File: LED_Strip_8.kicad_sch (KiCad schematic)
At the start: 8 parts

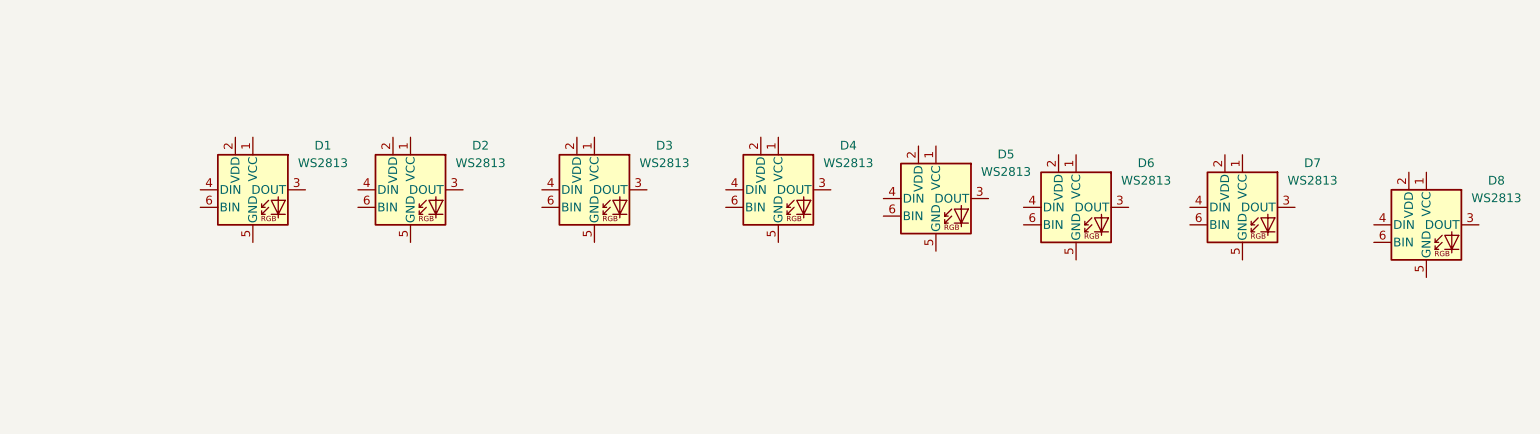
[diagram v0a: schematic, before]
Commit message: Wired LED strip
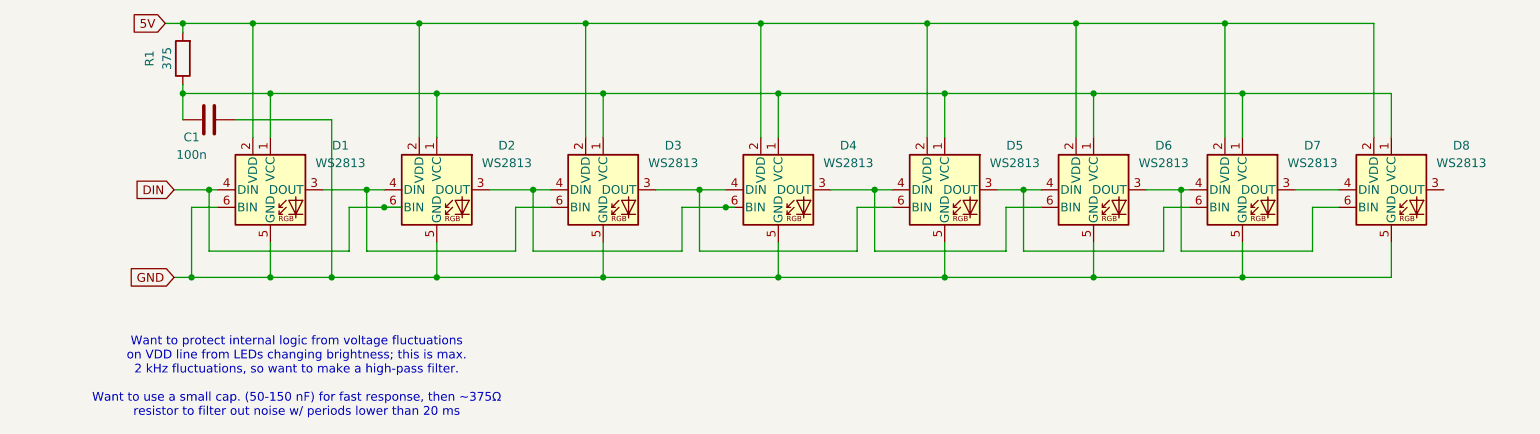
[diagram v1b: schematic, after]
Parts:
- added C1: 100n, symbol Device:C
- added R1: 375, symbol Device:R
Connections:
- net at D5.1 (VCC): now also D1.1 (VCC), D2.1 (VCC), D3.1 (VCC), D4.1 (VCC), D6.1 (VCC), D7.1 (VCC), D8.1 (VCC), C1.1, R1.1
- net 5V: now reaches D5.2 (VDD)
- net 5V: now also D1.2 (VDD), D2.2 (VDD), D3.2 (VDD), D4.2 (VDD), D6.2 (VDD), D7.2 (VDD), D8.2 (VDD), R1.2
- net at D5.3 (DOUT): now also D6.4 (DIN), D7.6 (BIN)
- net at D5.4 (DIN): now also D4.3 (DOUT), D6.6 (BIN)
- net GND: now reaches D5.5 (GND)
- net GND: now also D1.5 (GND), D1.6 (BIN), D2.5 (GND), D3.5 (GND), D4.5 (GND), D6.5 (GND), D7.5 (GND), D8.5 (GND), C1.2
- net at D5.6 (BIN): now also D3.3 (DOUT), D4.4 (DIN)
- net at D6.3 (DOUT): now also D7.4 (DIN), D8.6 (BIN)
- net at D3.4 (DIN): now also D2.3 (DOUT), D4.6 (BIN)
- net at D3.6 (BIN): now also D1.3 (DOUT), D2.4 (DIN)
- net at D8.4 (DIN): now also D7.3 (DOUT)
- net DIN: now reaches D1.4 (DIN)
- net DIN: now also D2.6 (BIN)
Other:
- note added: "Want to protect internal logic from voltage fluctuations on VDD line from LEDs changing brightness; this is max. 2 kHz fluctuations, so want to make a high-pass filter. Want to use a small cap. (50-150 nF) for fast response, then ~375Ω resistor to filter out noise w/ periods lower than 20 ms"
- moved on the sheet: D1, D2, D3, D5, D6, D7, D8

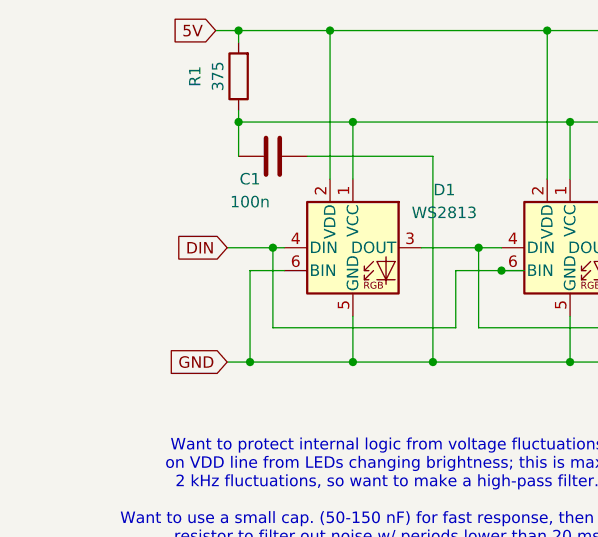
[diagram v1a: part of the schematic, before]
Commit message: Added regulators
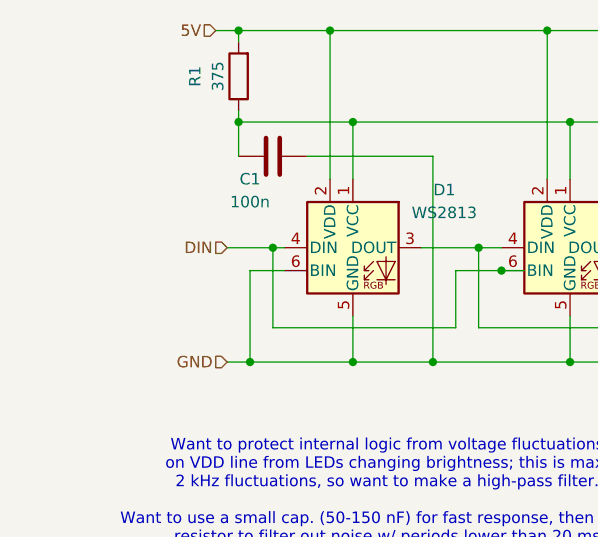
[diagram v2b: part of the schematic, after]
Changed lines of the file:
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@@
 		)
 	)
-	(global_label "5V"
+	(hierarchical_label "GND"
 		(shape input)
-		(at 38.1 33.02 180)
-		(fields_autoplaced yes)
+		(at 39.37 69.85 180)
 		(effects
 			(font
@@
 			(justify right)
 		)
-		(property "Intersheetrefs" "${INTERSHEET_REFS}"
-			(at 32.8167 33.02 0)
-			(effects
-				(font
-					(size 1.27 1.27)
-				)
-				(justify right)
-				(hide yes)
-			)
-		)
 	)
-	(global_label "GND"
+	(hierarchical_label "DIN"
 		(shape input)
-		(at 39.37 69.85 180)
-		(fields_autoplaced yes)
+		(at 39.37 57.15 180)
 		(effects
 			(font
@@
 			(justify right)
 		)
-		(property "Intersheetrefs" "${INTERSHEET_REFS}"
-			(at 32.5143 69.85 0)
-			(effects
-				(font
-					(size 1.27 1.27)
-				)
-				(justify right)
-				(hide yes)
-			)
-		)
 	)
-	(global_label "DIN"
+	(hierarchical_label "5V"
 		(shape input)
-		(at 39.37 57.15 180)
-		(fields_autoplaced yes)
+		(at 38.1 33.02 180)
 		(effects
 			(font
@@
 			(justify right)
 		)
-		(property "Intersheetrefs" "${INTERSHEET_REFS}"
-			(at 33.1795 57.15 0)
-			(effects
-				(font
-					(size 1.27 1.27)
-				)
-				(justify right)
-				(hide yes)
-			)
-		)
 	)
